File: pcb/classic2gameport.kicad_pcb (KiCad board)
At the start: 2 copper layers, 58 x 45 mm, 37 parts, among them J1 DB15_Male, J2 AVR-ISP-10, J3 Conn_01x04, Q1 Q_PMOS_GSD, Q2 Q_PMOS_GSD, Q3 Q_PMOS_GSD, Q4 Q_PMOS_GSD, Q5 Q_PMOS_GSD, Q6 Q_PMOS_GSD, Q7 Q_PMOS_GSD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

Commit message: Add LED
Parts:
- added D1: LED, LED_SMD:LED_1206_3216Metric, F.Cu at (160.5, 55.0)
- added R15: 1.2k, Resistor_SMD:R_0805_2012Metric_Pad1.15x1.40mm_HandSolder, F.Cu at (160.5, 61.0)
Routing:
- net Net-(C7-Pad1): track 45.4 -> 9.83 mm
- net 5V: track 200.6 -> 219.8 mm
- net JS2_Y2: track 48.8 -> 33.1 mm, vias 0 -> 1
- net BUTTON2: track 41.8 -> 56.1 mm
- net BUTTON4: track 39.8 -> 53.2 mm
- net MOSI: track 73.4 -> 62.2 mm
- net JS2_X_AXIS: track 32.9 -> 24.3 mm, vias 1 -> 0
- net BUTTON1: track 46.1 -> 38.1 mm
- net Net-(D1-Pad2): track 0.00 -> 7.51 mm
- net JS1_Y1: track 15.3 -> 19.6 mm, vias 1 -> 0
- net JS2_Y1: track 38.0 -> 33.7 mm, vias 3 -> 1
- net Net-(R15-Pad1): track 0.00 -> 3.98 mm
- net GND: track 161.2 -> 164.2 mm, vias 14 -> 1
- net BUTTON3: track 45.3 -> 42.4 mm
- net 3.3V: track 37.6 -> 40.1 mm
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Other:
- board text added: "1"
- board text added: "Classic2Gameport"
- board text added: "ISP"
- board text added: "V01"
- board text added: "github.com/TerrySoba/classic2gameport"

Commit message: Slightly change layout
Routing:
- net GND: track 164.2 -> 204.2 mm, vias 1 -> 0
- net 5V: track 219.8 -> 190.9 mm, vias 1 -> 2
- net BUTTON2: track 56.1 -> 49.7 mm
- net JS1_Y1: track 19.6 -> 24.3 mm, vias 0 -> 1
- net BUTTON3: track 42.4 -> 38.6 mm
- net BUTTON4: track 53.2 -> 50.4 mm
- net JS2_X_AXIS: track 24.3 -> 26.7 mm
- net 3.3V: track 40.1 -> 37.8 mm
- net JS1_X_AXIS: track 22.3 -> 24.4 mm
- net JS2_Y2: track 33.1 -> 35.1 mm
- net BUTTON1: track 38.1 -> 39.3 mm, vias 0 -> 1
- net Net-(Q6-Pad3): track 3.78 -> 4.81 mm
- net Net-(Q2-Pad3): track 4.81 -> 3.78 mm
- net JS2_X1: track 21.9 -> 22.6 mm
- net JS1_X2: track 19.8 -> 19.1 mm, vias 0 -> 2

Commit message: Add BOM
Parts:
- J2: footprint Connector_PinHeader_2.54mm:PinHeader_2x05_P2.54mm_Vertical -> Connector_Multicomp:Multicomp_MC9A12-1034_2x05_P2.54mm_Vertical
- turned J2 to 270 degrees
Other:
- board text removed: "1"
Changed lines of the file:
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@@
   (general
     (thickness 1.6)
-    (drawings 11)
+    (drawings 10)
     (tracks 403)
     (zones 0)
@@
     (add_net SDA)
   )
+  (module Connector_Multicomp:Multicomp_MC9A12-1034_2x05_P2.54mm_Vertical (layer F.Cu)
+    (at 205.5 62.5 270)
+    (descr http://www.farnell.com/datasheets/1520732.pdf)
+    (tags "connector multicomp MC9A MC9A12")
+    (fp_text reference J2 (at 1.27 -2.33 90) (layer F.SilkS)
+      (effects (font (size 1 1) (thickness 0.15)))
+    )
+    (fp_text value AVR-ISP-10 (at 1.27 12.49 90) (layer F.Fab)
+      (effects (font (size 1 1) (thickness 0.15)))
+    )
+    (fp_line (start 15.75 3.7) (end -5.55 3.7) (layer F.CrtYd) (width 0.05))
+    (fp_line (start 15.75 -6.25) (end 15.75 3.7) (layer F.CrtYd) (width 0.05))
+    (fp_line (start -5.55 -6.25) (end 15.75 -6.25) (layer F.CrtYd) (width 0.05))
+    (fp_line (start -5.55 3.7) (end -5.55 -6.25) (layer F.CrtYd) (width 0.05))
+    (fp_line (start -1.6 0) (end -2.2 0.6) (layer F.SilkS) (width 0.15))
+    (fp_line (start -2.2 -0.6) (end -1.6 0) (layer F.SilkS) (width 0.15))
+    (fp_line (start -2.2 0.6) (end -2.2 -0.6) (layer F.SilkS) (width 0.15))
+    (fp_line (start -2.65 -5.84) (end -2.15 -5.84) (layer F.SilkS) (width 0.15))
+    (fp_line (start -2.15 -5.94) (end -2.15 -5.74) (layer F.SilkS) (width 0.15))
+    (fp_line (start -2.65 -5.94) (end -2.15 -5.94) (layer F.SilkS) (width 0.15))
+    (fp_line (start -2.65 -5.74) (end -2.65 -5.94) (layer F.SilkS) (width 0.15))
+    (fp_line (start 12.31 -5.84) (end 12.81 -5.84) (layer F.SilkS) (width 0.15))
+    (fp_line (start 12.81 -5.94) (end 12.81 -5.74) (layer F.SilkS) (width 0.15))
+    (fp_line (start 12.31 -5.94) (end 12.81 -5.94) (layer F.SilkS) (width 0.15))
+    (fp_line (start 12.31 -5.74) (end 12.31 -5.94) (layer F.SilkS) (width 0.15))
+    (fp_line (start 4.83 -5.84) (end 5.33 -5.84) (layer F.SilkS) (width 0.15))
+    (fp_line (start 5.33 -5.94) (end 5.33 -5.74) (layer F.SilkS) (width 0.15))
+    (fp_line (start 4.83 -5.94) (end 5.33 -5.94) (layer F.SilkS) (width 0.15))
+    (fp_line (start 4.83 -5.74) (end 4.83 -5.94) (layer F.SilkS) (width 0.15))
+    (fp_line (start 7.305 1.9) (end 7.305 3.2) (layer F.SilkS) (width 0.15))
+    (fp_line (start 14.03 1.9) (end 7.305 1.9) (layer F.SilkS) (width 0.15))
+    (fp_line (start 14.03 -4.44) (end 14.03 1.9) (layer F.SilkS) (width 0.15))
+    (fp_line (start -3.87 -4.44) (end 14.03 -4.44) (layer F.SilkS) (width 0.15))
+    (fp_line (start -3.87 1.9) (end -3.87 -4.44) (layer F.SilkS) (width 0.15))
+    (fp_line (start 2.855 1.9) (end -3.87 1.9) (layer F.SilkS) (width 0.15))
+    (fp_line (start 2.855 3.2) (end 2.855 1.9) (layer F.SilkS) (width 0.15))
+    (fp_line (start 15.23 3.2) (end -5.07 3.2) (layer F.SilkS) (width 0.15))
+    (fp_line (start 15.23 -5.74) (end 15.23 3.2) (layer F.SilkS) (width 0.15))
+    (fp_line (start -5.07 -5.74) (end 15.23 -5.74) (layer F.SilkS) (width 0.15))
+    (fp_line (start -5.07 3.2) (end -5.07 -5.74) (layer F.SilkS) (width 0.15))
+    (fp_text user %R (at 1.27 5.08) (layer F.Fab)
+      (effects (font (size 1 1) (thickness 0.15)))
+    )
+    (pad 10 thru_hole circle (at 10.16 -2.54 270) (size 1.7 1.7) (drill 1) (layers *.Cu *.Mask)
+      (net 1 GND))
+    (pad 9 thru_hole circle (at 10.16 0 270) (size 1.7 1.7) (drill 1) (layers *.Cu *.Mask)
+      (net 15 MISO))
+    (pad 8 thru_hole circle (at 7.62 -2.54 270) (size 1.7 1.7) (drill 1) (layers *.Cu *.Mask)
+      (net 1 GND))
+    (pad 7 thru_hole circle (at 7.62 0 270) (size 1.7 1.7) (drill 1) (layers *.Cu *.Mask)
+      (net 16 SCK))
+    (pad 6 thru_hole circle (at 5.08 -2.54 270) (size 1.7 1.7) (drill 1) (layers *.Cu *.Mask)
+      (net 1 GND))
+    (pad 5 thru_hole circle (at 5.08 0 270) (size 1.7 1.7) (drill 1) (layers *.Cu *.Mask)
+      (net 17 RESET))
+    (pad 4 thru_hole circle (at 2.54 -2.54 270) (size 1.7 1.7) (drill 1) (layers *.Cu *.Mask)
+      (net 1 GND))
+    (pad 3 thru_hole circle (at 2.54 0 270) (size 1.7 1.7) (drill 1) (layers *.Cu *.Mask)
+      (net 18 "Net-(J2-Pad3)"))
+    (pad 2 thru_hole circle (at 0 -2.54 270) (size 1.7 1.7) (drill 1) (layers *.Cu *.Mask)
+      (net 3 5V))
+    (pad 1 thru_hole rect (at 0 0 270) (size 1.7 1.7) (drill 1) (layers *.Cu *.Mask)
+      (net 19 MOSI))
+    (model ${KISYS3DMOD}/Connector_Multicomp.3dshapes/Multicomp_MC9A12-1034_2x05_P2.54mm_Vertical.wrl
+      (at (xyz 0 0 0))
+      (scale (xyz 1 1 1))
+      (rotate (xyz 0 0 0))
+    )
+  )
   (module classic2gameport:G026 (layer F.Cu)
     (at 160.02 44.45)
@@
     )
   )
-  (module Connector_PinHeader_2.54mm:PinHeader_2x05_P2.54mm_Vertical (layer F.Cu)
-    (at 205.5 62.5)
-    (descr "Through hole straight pin header, 2x05, 2.54mm pitch, double rows")
-    (tags "Through hole pin header THT 2x05 2.54mm double row")
-    (fp_text reference J2 (at 1.27 -2.33) (layer F.SilkS)
-      (effects (font (size 1 1) (thickness 0.15)))
-    )
-    (fp_text value AVR-ISP-10 (at 1.27 12.49) (layer F.Fab)
-      (effects (font (size 1 1) (thickness 0.15)))
-    )
-    (fp_text user %R (at 1.27 5.08 90) (layer F.Fab)
-      (effects (font (size 1 1) (thickness 0.15)))
-    )
-    (fp_line (start 4.35 -1.8) (end -1.8 -1.8) (layer F.CrtYd) (width 0.05))
-    (fp_line (start 4.35 11.95) (end 4.35 -1.8) (layer F.CrtYd) (width 0.05))
-    (fp_line (start -1.8 11.95) (end 4.35 11.95) (layer F.CrtYd) (width 0.05))
-    (fp_line (start -1.8 -1.8) (end -1.8 11.95) (layer F.CrtYd) (width 0.05))
-    (fp_line (start -1.33 -1.33) (end 0 -1.33) (layer F.SilkS) (width 0.12))
-    (fp_line (start -1.33 0) (end -1.33 -1.33) (layer F.SilkS) (width 0.12))
-    (fp_line (start 1.27 -1.33) (end 3.87 -1.33) (layer F.SilkS) (width 0.12))
-    (fp_line (start 1.27 1.27) (end 1.27 -1.33) (layer F.SilkS) (width 0.12))
-    (fp_line (start -1.33 1.27) (end 1.27 1.27) (layer F.SilkS) (width 0.12))
-    (fp_line (start 3.87 -1.33) (end 3.87 11.49) (layer F.SilkS) (width 0.12))
-    (fp_line (start -1.33 1.27) (end -1.33 11.49) (layer F.SilkS) (width 0.12))
-    (fp_line (start -1.33 11.49) (end 3.87 11.49) (layer F.SilkS) (width 0.12))
-    (fp_line (start -1.27 0) (end 0 -1.27) (layer F.Fab) (width 0.1))
-    (fp_line (start -1.27 11.43) (end -1.27 0) (layer F.Fab) (width 0.1))
-    (fp_line (start 3.81 11.43) (end -1.27 11.43) (layer F.Fab) (width 0.1))
-    (fp_line (start 3.81 -1.27) (end 3.81 11.43) (layer F.Fab) (width 0.1))
-    (fp_line (start 0 -1.27) (end 3.81 -1.27) (layer F.Fab) (width 0.1))
-    (pad 10 thru_hole oval (at 2.54 10.16) (size 1.7 1.7) (drill 1) (layers *.Cu *.Mask)
-      (net 1 GND))
-    (pad 9 thru_hole oval (at 0 10.16) (size 1.7 1.7) (drill 1) (layers *.Cu *.Mask)
-      (net 15 MISO))
-    (pad 8 thru_hole oval (at 2.54 7.62) (size 1.7 1.7) (drill 1) (layers *.Cu *.Mask)
-      (net 1 GND))
-    (pad 7 thru_hole oval (at 0 7.62) (size 1.7 1.7) (drill 1) (layers *.Cu *.Mask)
-      (net 16 SCK))
-    (pad 6 thru_hole oval (at 2.54 5.08) (size 1.7 1.7) (drill 1) (layers *.Cu *.Mask)
-      (net 1 GND))
-    (pad 5 thru_hole oval (at 0 5.08) (size 1.7 1.7) (drill 1) (layers *.Cu *.Mask)
-      (net 17 RESET))
-    (pad 4 thru_hole oval (at 2.54 2.54) (size 1.7 1.7) (drill 1) (layers *.Cu *.Mask)
-      (net 1 GND))
-    (pad 3 thru_hole oval (at 0 2.54) (size 1.7 1.7) (drill 1) (layers *.Cu *.Mask)
-      (net 18 "Net-(J2-Pad3)"))
-    (pad 2 thru_hole oval (at 2.54 0) (size 1.7 1.7) (drill 1) (layers *.Cu *.Mask)
-      (net 3 5V))
-    (pad 1 thru_hole rect (at 0 0) (size 1.7 1.7) (drill 1) (layers *.Cu *.Mask)
-      (net 19 MOSI))
-    (model ${KISYS3DMOD}/Connector_PinHeader_2.54mm.3dshapes/PinHeader_2x05_P2.54mm_Vertical.wrl
-      (at (xyz 0 0 0))
-      (scale (xyz 1 1 1))
-      (rotate (xyz 0 0 0))
-    )
-  )
   (module Connector_Dsub:DSUB-15_Male_Horizontal_P2.77x2.84mm_EdgePinOffset4.94mm_Housed_MountingHolesOffset7.48mm (layer F.Cu)
     (at 194.31 46.99 180)
@@
     )
   )
-  (gr_text 1 (at 203 62.5) (layer F.SilkS)
-    (effects (font (size 1 1) (thickness 0.15)))
-  )
-  (gr_text ISP (at 211 68 270) (layer F.SilkS)
+  (gr_text ISP (at 212.5 67.5 270) (layer F.SilkS)
     (effects (font (size 1 1) (thickness 0.15)))
   )
@@
     (effects (font (size 1.5 1.5) (thickness 0.3)) (justify mirror))
   )
-  (gr_text Classic2Gameport (at 194.5 55) (layer F.SilkS)
+  (gr_text Classic2Gameport (at 198 52) (layer F.SilkS)
     (effects (font (size 1 1) (thickness 0.15)))
   )
-  (gr_text github.com/TerrySoba/classic2gameport (at 195.5 57) (layer F.SilkS)
+  (gr_text github.com/TerrySoba/classic2gameport (at 195.5 55.5) (layer F.SilkS)
     (effects (font (size 1 1) (thickness 0.15)))
   )

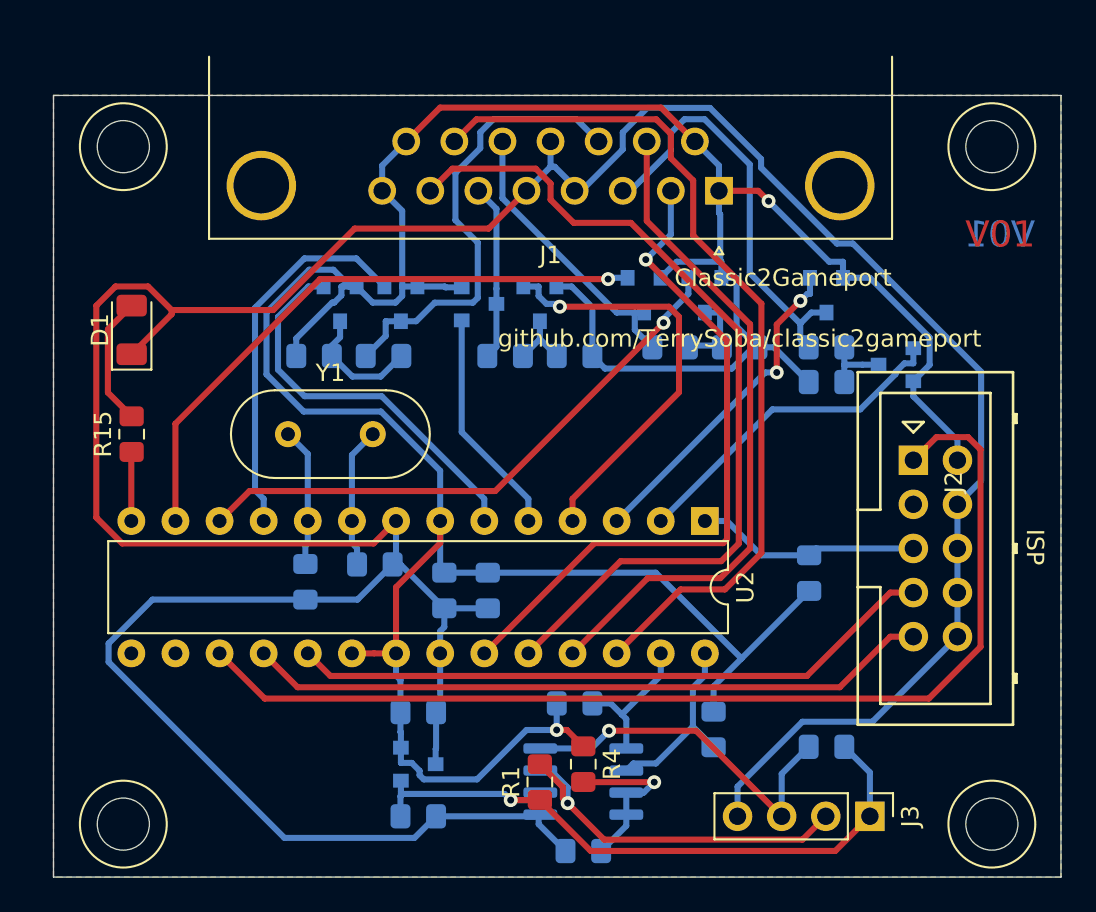
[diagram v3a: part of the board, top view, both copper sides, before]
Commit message: Change some footprints
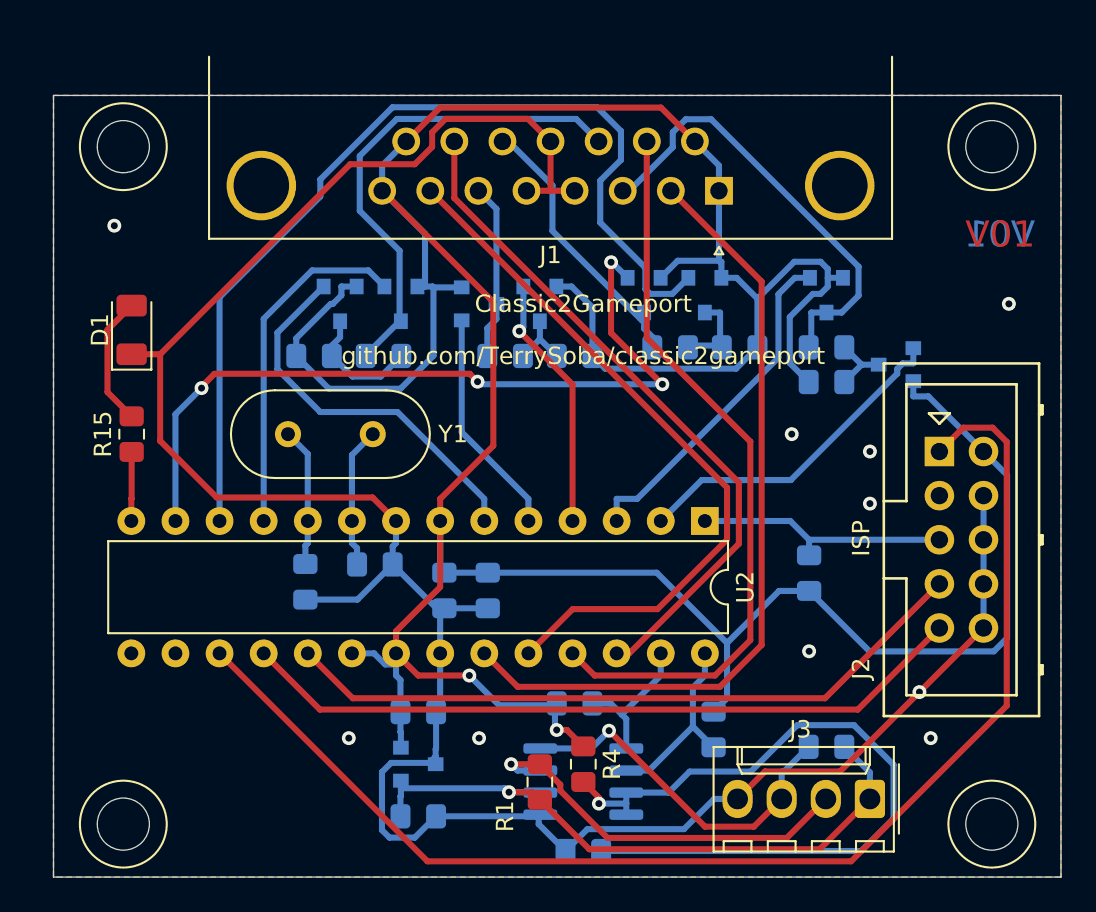
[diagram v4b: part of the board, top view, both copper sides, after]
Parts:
- J3: footprint Connector_PinHeader_2.54mm:PinHeader_1x04_P2.54mm_Vertical -> Connector_Molex:Molex_KK-254_AE-6410-04A_1x04_P2.54mm_Vertical
- moved J2 1.58 mm to (207.0, 62.0)
- moved J3 1.00 mm to (203.0, 82.0), turned to 180 degrees
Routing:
- net GND: track 204.2 -> 137.1 mm, vias 0 -> 10
- net Net-(C7-Pad1): track 9.91 -> 43.1 mm
- net 5V: track 190.9 -> 213.5 mm
- net JS2_Y1: track 33.5 -> 55.3 mm, vias 1 -> 0
- net MOSI: track 62.2 -> 74.0 mm
- net BUTTON4: track 50.4 -> 39.6 mm
- net JS2_Y2: track 35.1 -> 45.0 mm, vias 1 -> 4
- net JS1_Y1: track 24.3 -> 14.9 mm
- net BUTTON2: track 49.7 -> 41.3 mm
- net BUTTON1: track 39.3 -> 46.1 mm, vias 1 -> 0
- net BUTTON3: track 38.6 -> 42.8 mm
- net MISO: track 39.4 -> 42.2 mm
- net SCK: track 37.4 -> 40.2 mm
- net JS2_X_AXIS: track 26.7 -> 28.5 mm
- net RESET: track 13.0 -> 14.8 mm
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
